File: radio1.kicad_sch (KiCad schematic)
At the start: 27 parts, among them Y1 OW2EL89CENUXK7YLC-40M

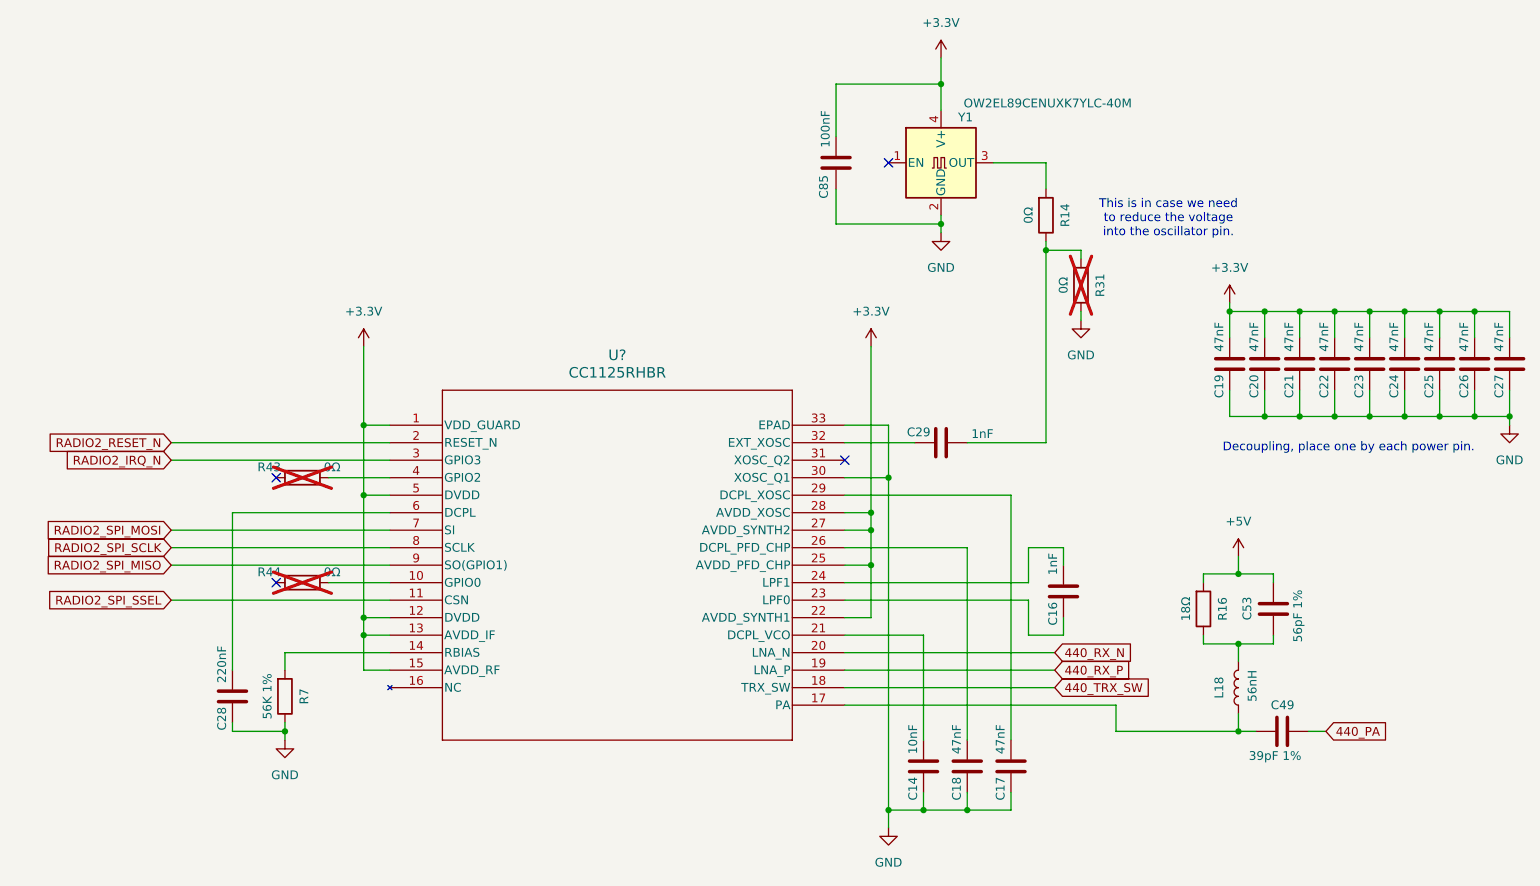
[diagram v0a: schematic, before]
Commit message: First start at reworking to get HDLC
Signed-off-by: Corey Minyard <corey@minyard.net>
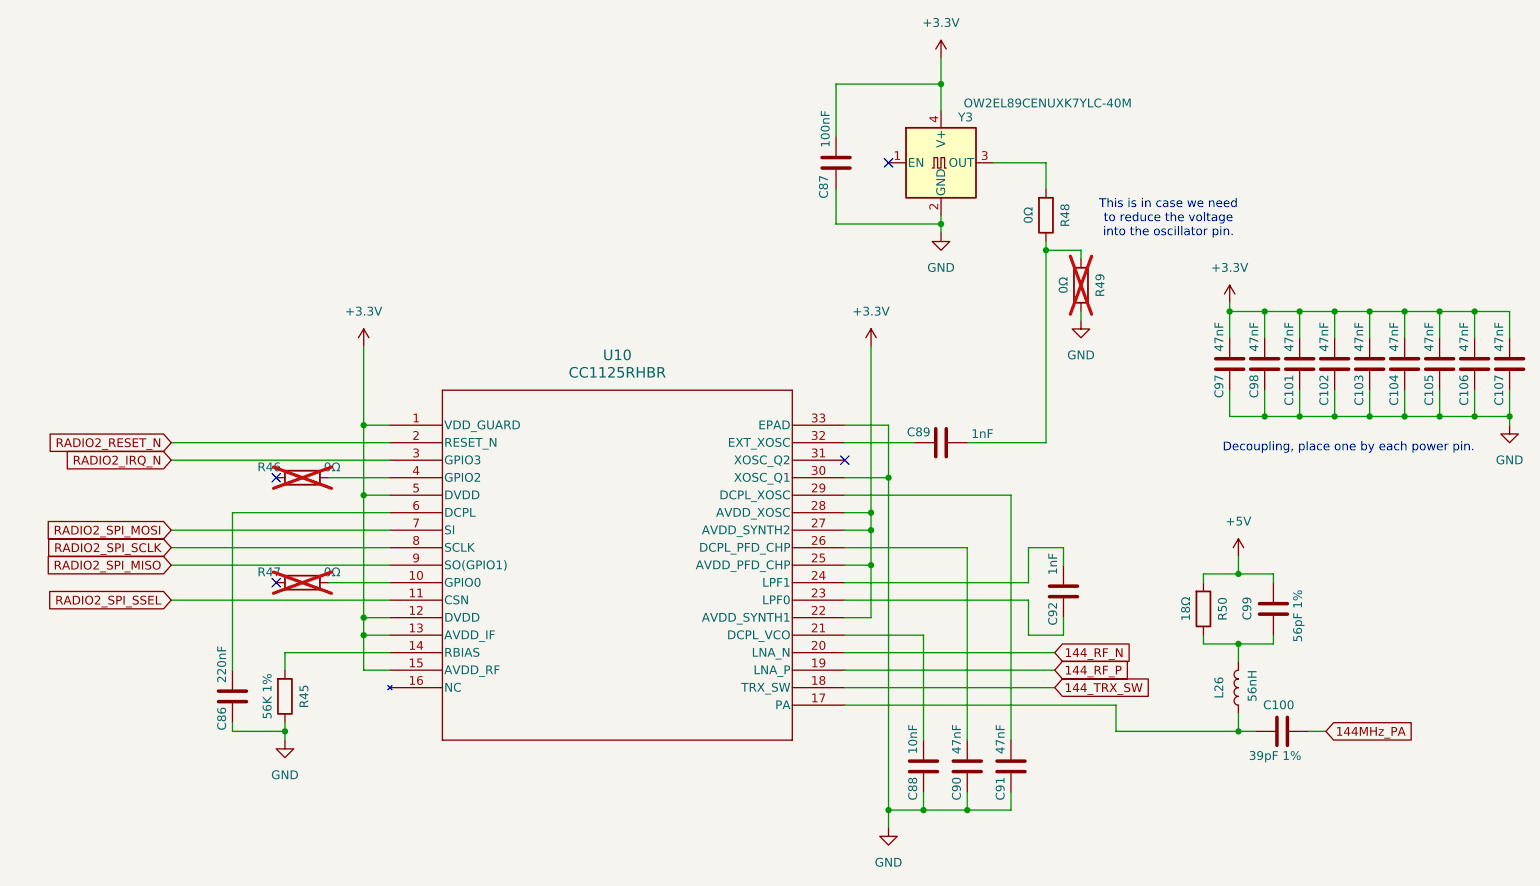
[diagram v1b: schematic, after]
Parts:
- gave numbers to parts that had none: 1
- renumbered C49 to C100, C21 to C101, C22 to C102, C23 to C103, C24 to C104, C25 to C105, C26 to C106, C27 to C107, C28 to C86, C85 to C87, C14 to C88, C29 to C89, C18 to C90, C17 to C91, C16 to C92, C19 to C97, C20 to C98, C53 to C99, L18 to L26, R7 to R45, R43 to R46, R44 to R47, R14 to R48, R31 to R49, R16 to R50, Y1 to Y3
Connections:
- net 440_PA renamed 144MHz_PA
- net 440_RX_N renamed 144_RF_N
- net 440_RX_P renamed 144_RF_P
- net 440_TRX_SW renamed 144_TRX_SW

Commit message: More re-layout for the new design
Signed-off-by: Corey Minyard <corey@minyard.net>
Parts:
- removed R46, R47: 0Ω, Resistor_SMD:R_0402_1005Metric, symbol Device:R
- removed R50: 18Ω, Resistor_SMD:R_0402_1005Metric, symbol Device:R
- added C125: 10nF, Capacitor_SMD:C_0402_1005Metric_Pad0.74x0.62mm_HandSolder, symbol Device:C
- C100: value 39pF 1% -> 82pF 1%
- C99: value 56pF 1% -> 100pF
- L26: value 56nH -> 220nH
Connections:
- net +5V is gone; now on net +3.3V: C99.2
- net +3.3V: now also L26.2, C125.2
- net GND: now also C99.1, C125.1
- net RADIO1_GPIO2: now reaches U10.4 (GPIO2)
- net RADIO1_GPIO0: now reaches U10.10 (GPIO0)
- net 144MHz_PA renamed 144_PA
- net RADIO2_IRQ_N renamed RADIO1_GPIO3
- net RADIO2_RESET_N renamed RADIO1_RESET_N
- net RADIO2_SPI_MISO renamed RADIO_SPI_MISO
- net RADIO2_SPI_MOSI renamed RADIO_SPI_MOSI
- net RADIO2_SPI_SCLK renamed RADIO_SPI_SCLK
- net RADIO2_SPI_SSEL renamed RADIO1_SPI_SSEL
- no-connect marks 4 -> 2
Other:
- moved on the sheet: C99

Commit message: Add some vias
Signed-off-by: Corey Minyard <corey@minyard.net>
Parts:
- L26: footprint Inductor_SMD:L_0603_1608Metric_Pad1.05x0.95mm_HandSolder -> Inductor_SMD:L_0805_2012Metric_Pad1.05x1.20mm_HandSolder
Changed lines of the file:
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@@
 			)
 		)
-		(property "Footprint" "Inductor_SMD:L_0603_1608Metric_Pad1.05x0.95mm_HandSolder"
+		(property "Footprint" "Inductor_SMD:L_0805_2012Metric_Pad1.05x1.20mm_HandSolder"
 			(at 214.63 113.03 0)
 			(effects
